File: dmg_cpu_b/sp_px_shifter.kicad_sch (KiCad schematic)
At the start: 89 parts

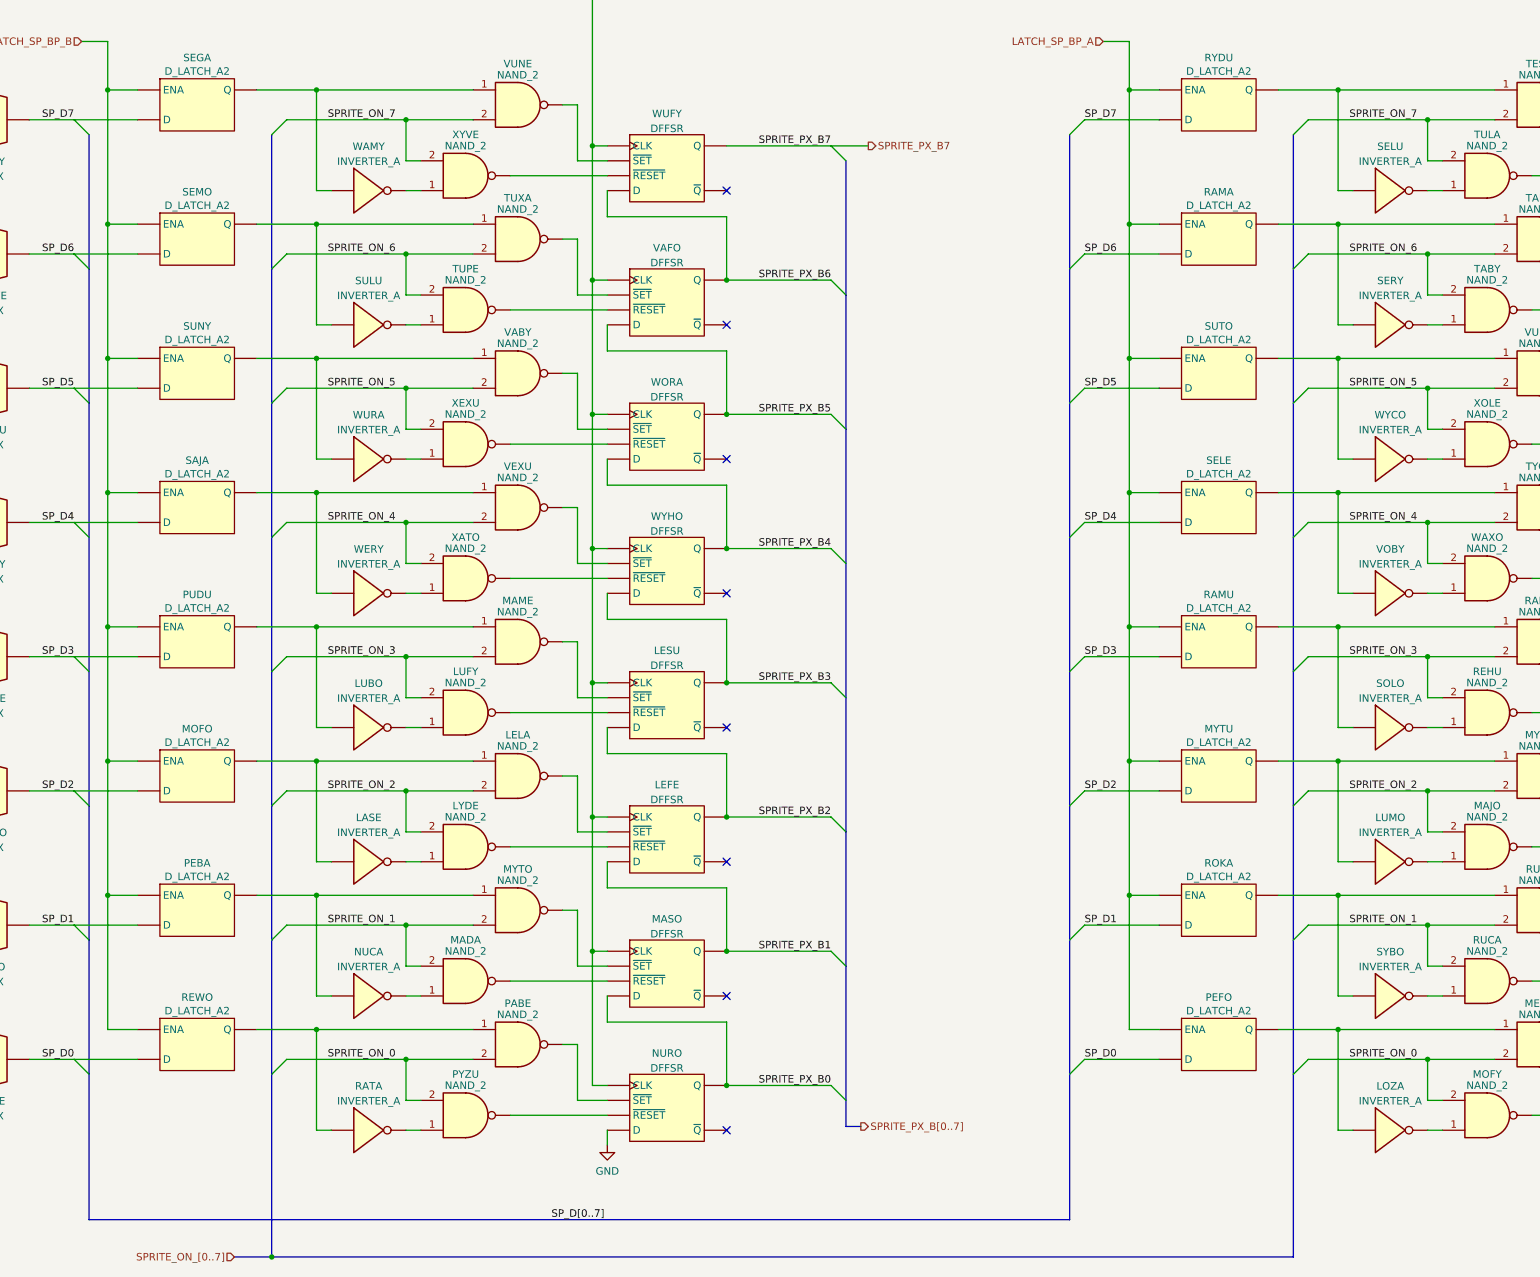
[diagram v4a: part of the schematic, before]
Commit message: Issues addressed. Renaming and inverted signal names to make thing more consistent and meaningful.
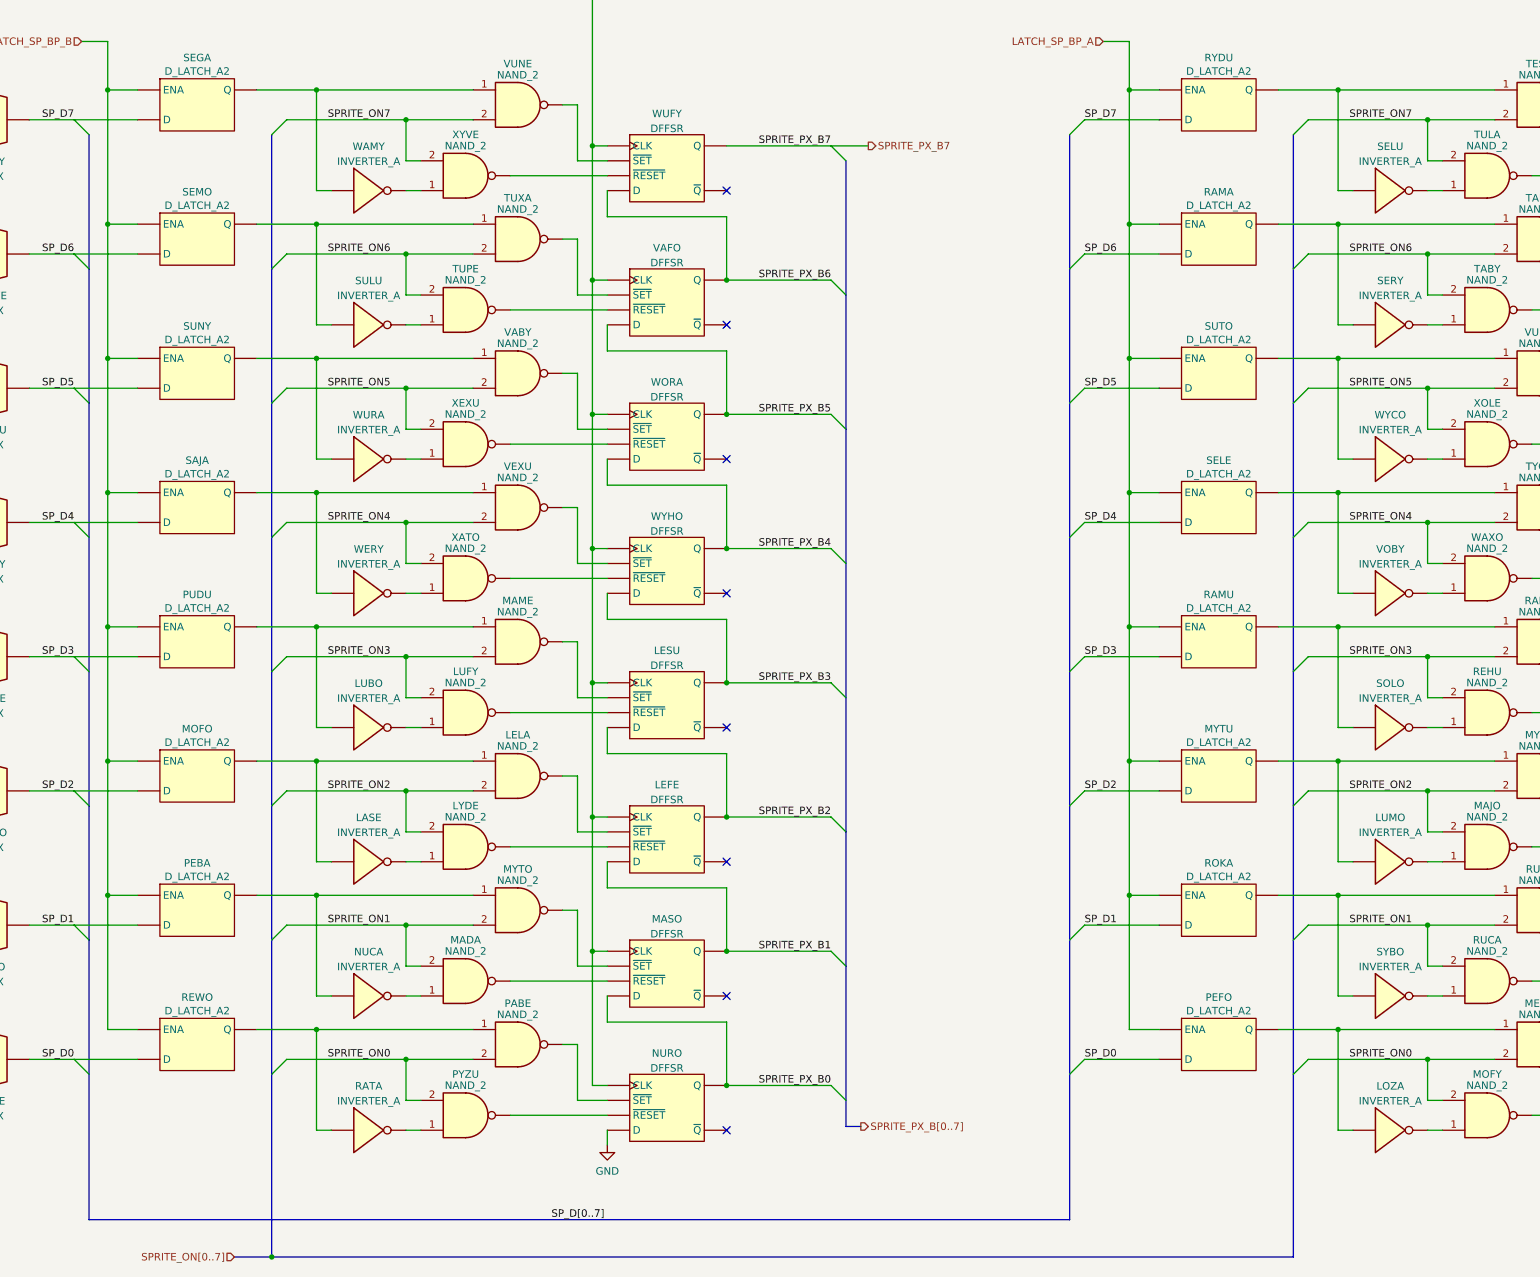
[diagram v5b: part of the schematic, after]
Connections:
- net SPRITE_ON_0 renamed SPRITE_ON0
- net SPRITE_ON_1 renamed SPRITE_ON1
- net SPRITE_ON_2 renamed SPRITE_ON2
- net SPRITE_ON_3 renamed SPRITE_ON3
- net SPRITE_ON_4 renamed SPRITE_ON4
- net SPRITE_ON_5 renamed SPRITE_ON5
- net SPRITE_ON_6 renamed SPRITE_ON6
- net SPRITE_ON_7 renamed SPRITE_ON7
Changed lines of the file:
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@@
     (effects (font (size 1.27 1.27)) (justify right bottom))
   )
-  (label "SPRITE_ON_2" (at 120.015 173.355 0)
+  (label "SPRITE_ON2" (at 120.015 173.355 0)
     (effects (font (size 1.27 1.27)) (justify left bottom))
   )
@@
     (effects (font (size 1.27 1.27)) (justify right bottom))
   )
-  (label "SPRITE_ON_1" (at 294.005 196.215 0)
+  (label "SPRITE_ON1" (at 294.005 196.215 0)
     (effects (font (size 1.27 1.27)) (justify left bottom))
   )
@@
     (effects (font (size 1.27 1.27)) (justify right bottom))
   )
-  (label "SPRITE_ON_5" (at 294.005 104.775 0)
+  (label "SPRITE_ON5" (at 294.005 104.775 0)
     (effects (font (size 1.27 1.27)) (justify left bottom))
   )
@@
     (effects (font (size 1.27 1.27)) (justify left bottom))
   )
-  (label "SPRITE_ON_1" (at 120.015 196.215 0)
+  (label "SPRITE_ON1" (at 120.015 196.215 0)
     (effects (font (size 1.27 1.27)) (justify left bottom))
   )
@@
     (effects (font (size 1.27 1.27)) (justify right bottom))
   )
-  (label "SPRITE_ON_3" (at 294.005 150.495 0)
+  (label "SPRITE_ON3" (at 294.005 150.495 0)
     (effects (font (size 1.27 1.27)) (justify left bottom))
   )
@@
     (effects (font (size 1.27 1.27)) (justify right bottom))
   )
-  (label "SPRITE_ON_3" (at 120.015 150.495 0)
+  (label "SPRITE_ON3" (at 120.015 150.495 0)
     (effects (font (size 1.27 1.27)) (justify left bottom))
   )
@@
     (effects (font (size 1.27 1.27)) (justify left bottom))
   )
-  (label "SPRITE_ON_0" (at 294.005 219.075 0)
-    (effects (font (size 1.27 1.27)) (justify left bottom))
-  )
-  (label "SPRITE_ON_0" (at 120.015 219.075 0)
+  (label "SPRITE_ON0" (at 294.005 219.075 0)
+    (effects (font (size 1.27 1.27)) (justify left bottom))
+  )
+  (label "SPRITE_ON0" (at 120.015 219.075 0)
     (effects (font (size 1.27 1.27)) (justify left bottom))
   )
@@
     (effects (font (size 1.27 1.27)) (justify left bottom))
   )
-  (label "SPRITE_ON_4" (at 294.005 127.635 0)
+  (label "SPRITE_ON4" (at 294.005 127.635 0)
     (effects (font (size 1.27 1.27)) (justify left bottom))
   )
@@
     (effects (font (size 1.27 1.27)) (justify right bottom))
   )
-  (label "SPRITE_ON_4" (at 120.015 127.635 0)
-    (effects (font (size 1.27 1.27)) (justify left bottom))
-  )
-  (label "SPRITE_ON_5" (at 120.015 104.775 0)
+  (label "SPRITE_ON4" (at 120.015 127.635 0)
+    (effects (font (size 1.27 1.27)) (justify left bottom))
+  )
+  (label "SPRITE_ON5" (at 120.015 104.775 0)
     (effects (font (size 1.27 1.27)) (justify left bottom))
   )
@@
     (effects (font (size 1.27 1.27)) (justify right bottom))
   )
-  (label "SPRITE_ON_6" (at 120.015 81.915 0)
+  (label "SPRITE_ON6" (at 120.015 81.915 0)
     (effects (font (size 1.27 1.27)) (justify left bottom))
   )
@@
     (effects (font (size 1.27 1.27)) (justify left bottom))
   )
-  (label "SPRITE_ON_2" (at 294.005 173.355 0)
-    (effects (font (size 1.27 1.27)) (justify left bottom))
-  )
-  (label "SPRITE_ON_7" (at 294.005 59.055 0)
-    (effects (font (size 1.27 1.27)) (justify left bottom))
-  )
-  (label "SPRITE_ON_7" (at 120.015 59.055 0)
+  (label "SPRITE_ON2" (at 294.005 173.355 0)
+    (effects (font (size 1.27 1.27)) (justify left bottom))
+  )
+  (label "SPRITE_ON7" (at 294.005 59.055 0)
+    (effects (font (size 1.27 1.27)) (justify left bottom))
+  )
+  (label "SPRITE_ON7" (at 120.015 59.055 0)
     (effects (font (size 1.27 1.27)) (justify left bottom))
   )
@@
     (effects (font (size 1.27 1.27)) (justify left bottom))
   )
-  (label "SPRITE_ON_6" (at 294.005 81.915 0)
+  (label "SPRITE_ON6" (at 294.005 81.915 0)
     (effects (font (size 1.27 1.27)) (justify left bottom))
   )
@@
     (effects (font (size 1.27 1.27)) (justify right))
   )
-  (hierarchical_label "SPRITE_ON_[0..7]" (shape input) (at 104.14 252.73 180)
-    (effects (font (size 1.27 1.27)) (justify right))
-  )
+  (hierarchical_label "SPRITE_ON[0..7]" (shape input) (at 104.14 252.73 180)
+    (effects (font (size 1.27 1.27)) (justify right))
+  )
